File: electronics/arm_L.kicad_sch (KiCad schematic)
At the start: 26 parts, among them J11 EV3 L 4434 HOLD, J21 L SERVO G + S, U11 DRV8871DDAR, U21 SN74LVC2G17DBVR, U31 SN74AHCT1G125DBVR

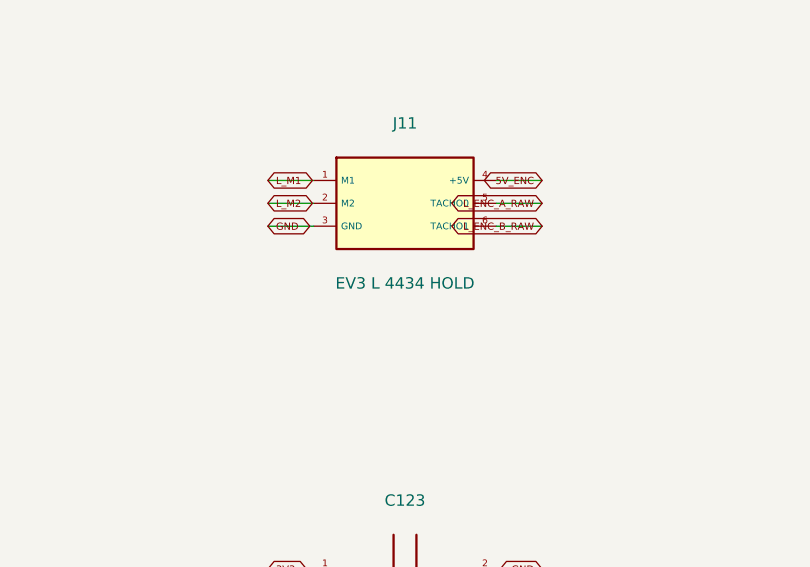
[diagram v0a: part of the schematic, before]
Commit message: Integrate onboard RP2040 and drawing-based EV3 jacks on A1 PCB
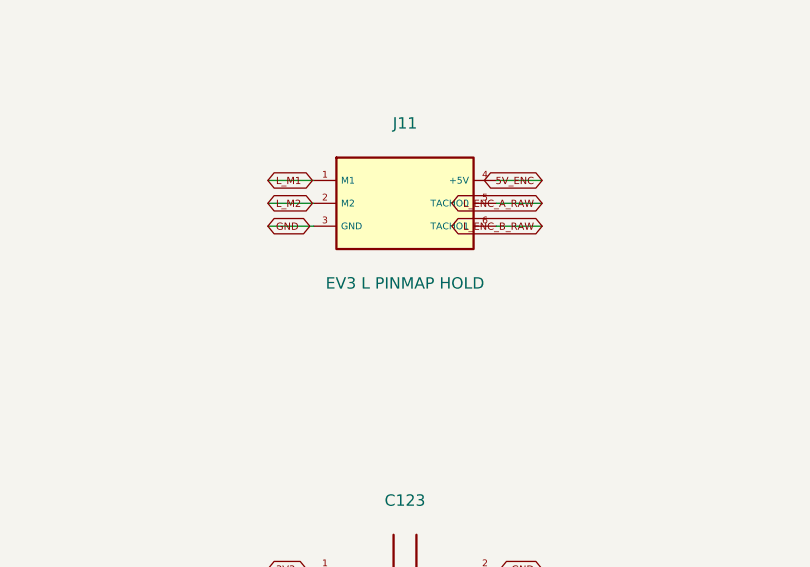
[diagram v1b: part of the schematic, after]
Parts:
- J11: value EV3 L 4434 HOLD -> EV3 L PINMAP HOLD; footprint Quadcuber:EV3_4434_PROVISIONAL -> Quadcuber:EV3_UserDrawing_PINMAP_HOLD; MPN 4434 -> UNCONFIRMED user drawing; Manufacturer Adafruit (supplier brand) -> Unconfirmed (Coorle watermark)
- TP14, TP15, TP16, TP17: now left out of the parts list
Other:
- title: Quadcuber A0 / arm_L / ENGINEERING HOLD -> Quadcuber A1 / arm_L / ENGINEERING HOLD

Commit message: Correct audited power BOM and add bounded VM discharge protection
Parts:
- C121: MPN GRM32ER71E106KA12L -> GRM32DR71E106KA12L
- F11: footprint Quadcuber:Fuse_1812_4532Metric -> Quadcuber:Fuse_Bourns_MF_MSMF_Style2_1812; MPN MF-MSMF110-2 -> MF-MSMF110/16X-2

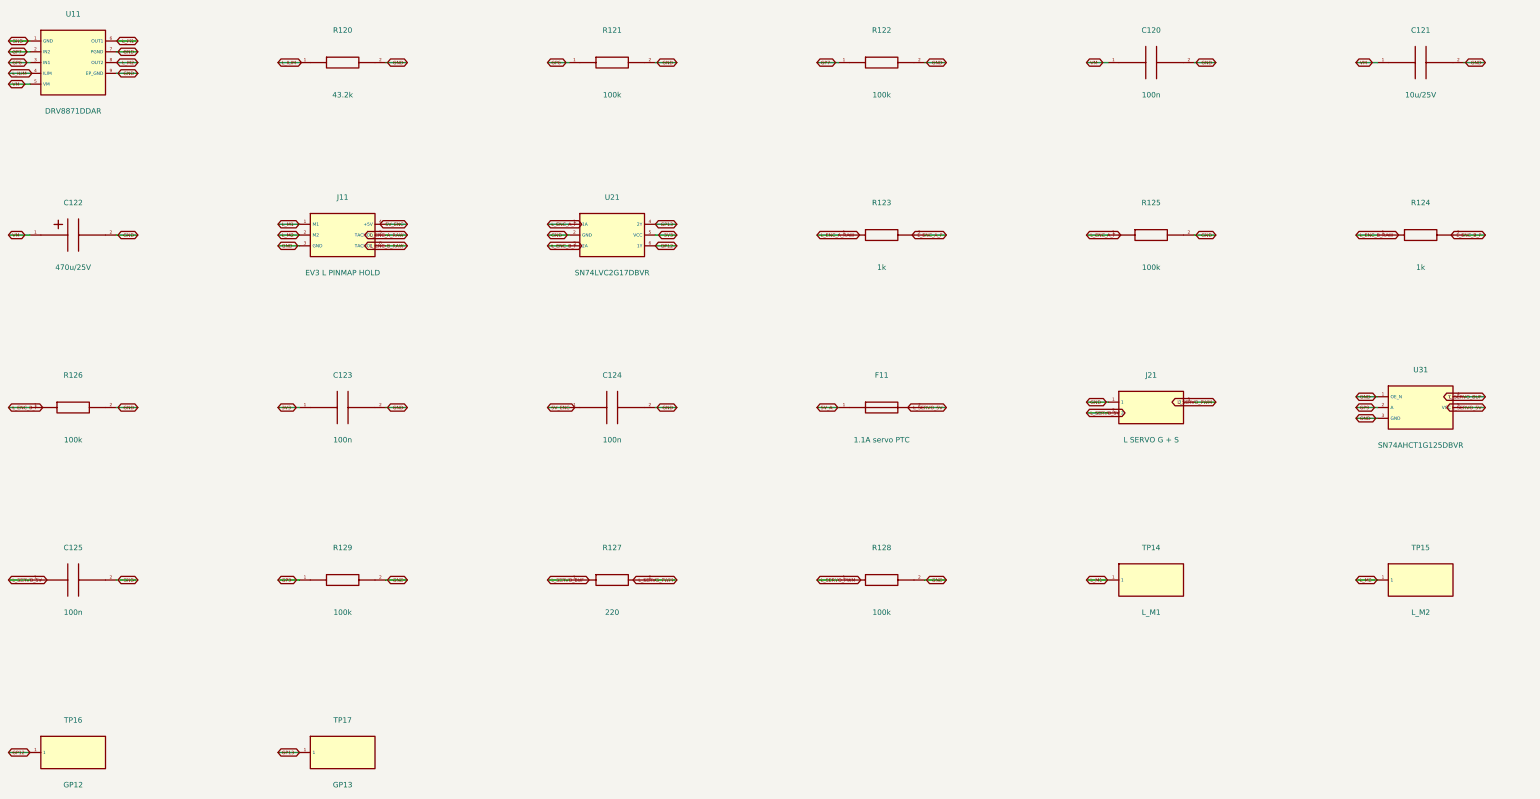
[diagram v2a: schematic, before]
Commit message: Migrate A1 to KiCad 10 and record blocked vendor-model transients
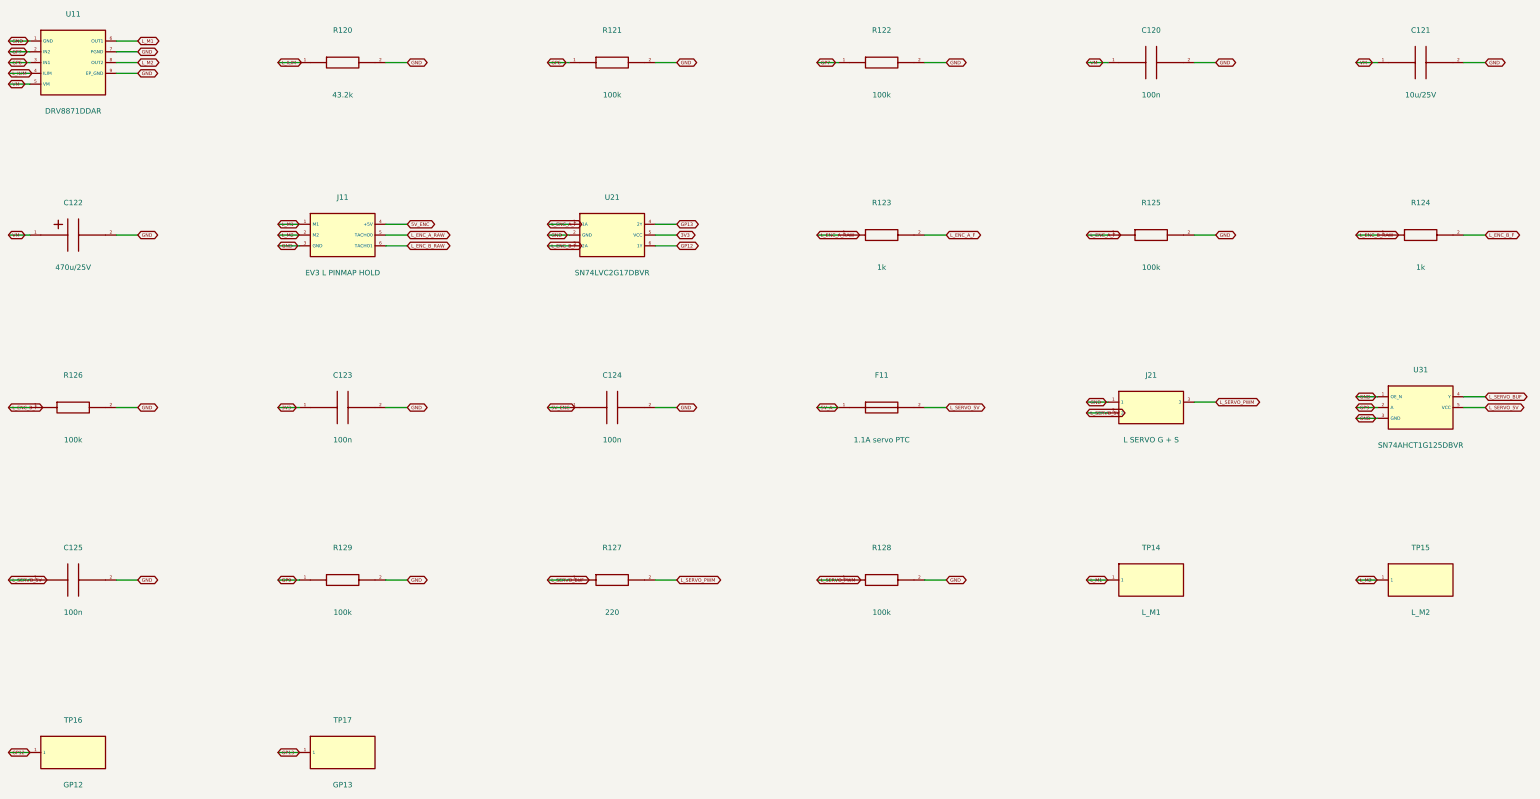
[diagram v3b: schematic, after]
